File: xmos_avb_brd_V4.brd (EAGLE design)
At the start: 80 x 40 mm, 143 parts, among them IC1 IS25LP080D-JULE-TR_IS25LP080D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, J1 0826-1X1T-KL-F_0826-1X1T-KL-F, U1 AG9900_AG9905LP, U10 ST-MICROELECTRONICS2_ST1S06PUR, U2 AR8035_AR8035-AL1A-R, U3 XE216-512-TQ128-C20_XE216-512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, U4 ADM1085AKSZ-REEL7_ADM1085AKSZ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, U5 NC7WZ07P6X_NC7WZ07P6X, U6 CS2100-CP_CS2100-CP-CZZ, U7 ST-MICROELECTRONICS2_ST1S06PUR, U8 NCP303LSN30, U9 MIC5213-2.5V, X1 FA-238 25.000, X2 TC2050-XTAG_TC2050-NL-MCP-NL, X3 CON-MOLEX_52559-3092, X4 CON-MOLEX_52559-0692, Y1 ECS-3225Q-33-240-DP-TR_ECS-32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

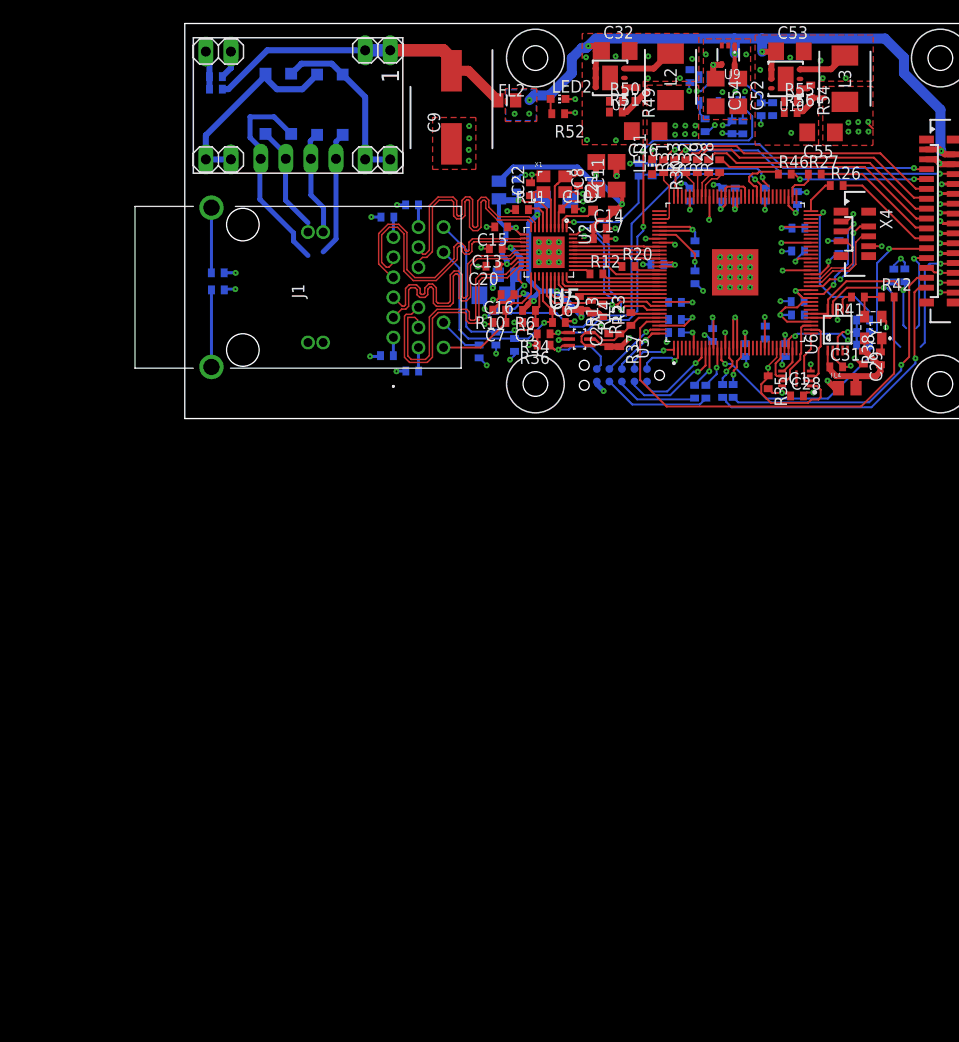
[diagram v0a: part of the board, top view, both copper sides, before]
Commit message: new debug header added to improve debugging with xmos. old tag-connect removed.
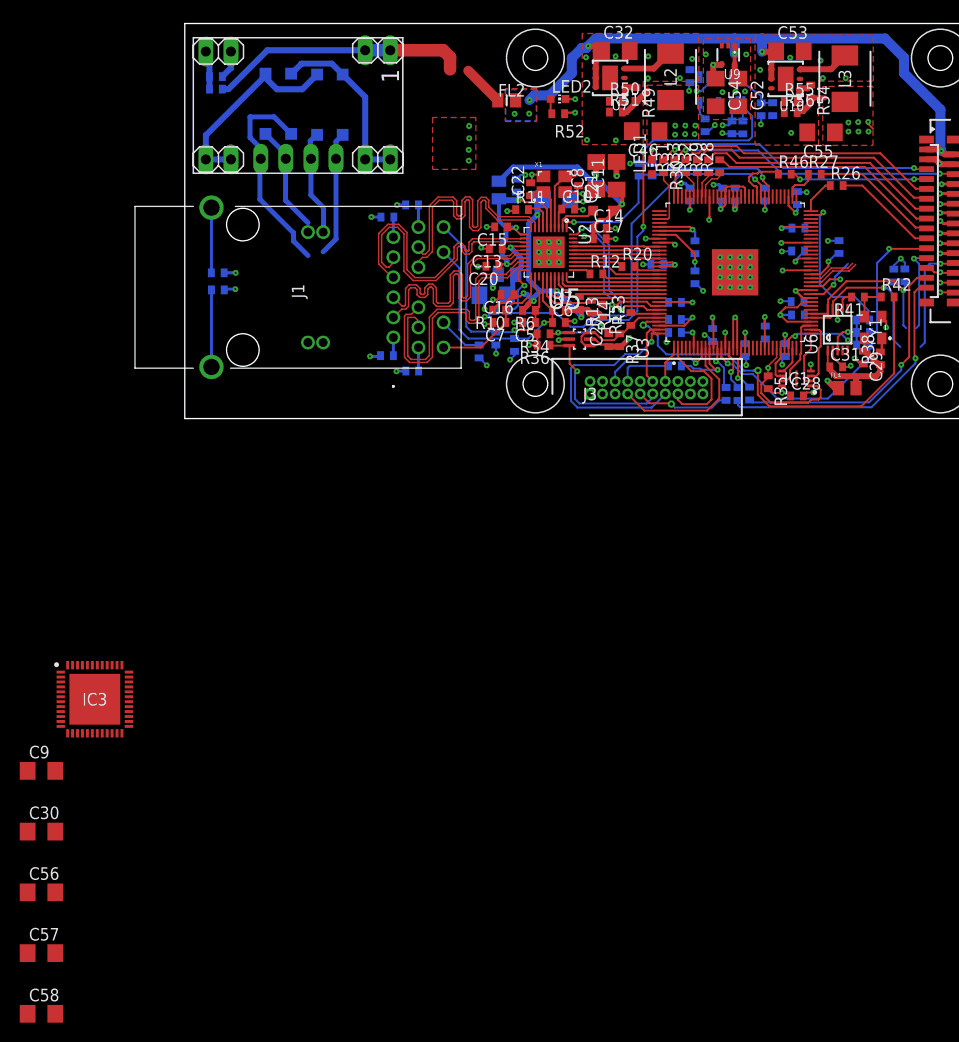
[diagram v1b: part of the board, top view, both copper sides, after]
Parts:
- removed X2: TC2050-XTAG_TC2050-NL-MCP-NL, xmos_avb_brd_V4:TC2050-XTAG_TC2030-MCP-NL
- removed X4: CON-MOLEX_52559-0692, xmos_avb_brd_V4:CON-MOLEX_52559-0692
- added C30, C56, C57, C58: 1u, xmos_avb_brd_V4:RCL_C1206
- added IC3: KSZ9131RNXI-TR, KSZ9131RNXI-TR:QFN50P700X700X90-49N
- added J3: ESHF-110-01-L-D-TH, ESHF-110-01-L-D-TH:SHDR20W41P127_2X10_1905X559X54
- C9: value EEH-ZC1V101P_EEH-ZC1V101P -> 1u; device xmos_avb_brd_V4:EEH-ZC1V101P_CAPAE830X1050N -> xmos_avb_brd_V4:RCL_C1206
- moved C9 79.0 mm to (-14.5, -35.7), turned to 0 degrees
- moved R24 3.29 mm to (49.6, 5.34), turned to 0 degrees
- moved R25 2.06 mm to (54.8, 2.50)
- moved R47 1.68 mm to (57.2, 2.52)
- moved R48 1.58 mm to (56.0, 2.48)
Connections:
- net GND: now also C30.2, C56.2, C57.2, C58.2, J3.10, J3.18, J3.3; no longer X2.5, X4.1, X4.6
- net TCK: now also J3.13; no longer X2.8
- net TDI: now also J3.15; no longer X2.10
- net TDO: now also J3.14; no longer X2.9
- net TMS: now also J3.12; no longer X2.7
- net USB_DM_N: now also J3.20; no longer X4.5
- net USB_DP_P: now also J3.19; no longer X4.4
- net USB_ID: now also J3.17; no longer X4.3
- net USB_VBUS: now also J3.16; no longer X4.2
- net VDC: now also C30.1, C56.1, C57.1, C58.1
- net XL_DN0: now also J3.7; no longer X2.2
- net XL_DN1: now also J3.6; no longer X2.1
- net XL_UP0: now also J3.8; no longer X2.3
- net XL_UP1: now also J3.9; no longer X2.4
- net XSYS_RST_N: now also J3.11; no longer X2.6
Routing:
- net TCK: track 5.63 -> 24.6 mm
- net XSYS_RST_N: track 8.57 -> 16.5 mm
- net USB_VBUS: track 10.3 -> 3.26 mm, vias 2 -> 1
- net TDI: track 5.18 -> 11.7 mm, vias 1 -> 0
- net USB_ID: track 11.3 -> 5.40 mm, vias 2 -> 1
- net GND: track 91.4 -> 86.1 mm, vias 112 -> 109
- net XL_DN0: track 11.0 -> 16.2 mm, vias 1 -> 0
- net USB_DP_P: track 9.08 -> 5.29 mm
- net XL_DN1: track 8.62 -> 11.7 mm
- net USB_DM_N: track 7.93 -> 4.88 mm
- net XL_UP0: track 8.31 -> 5.59 mm
- net N$43: track 4.49 -> 6.50 mm
- net VDC: track 32.4 -> 30.5 mm
- net SDIOE_OUT: track 29.5 -> 27.8 mm
- net TDO: track 5.50 -> 3.92 mm, vias 1 -> 0
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
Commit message: ksz9131 added to schematic.#
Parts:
- removed C16: 100n, xmos_avb_brd_V4:RCL_C0402
- removed C18, C19: 1u, xmos_avb_brd_V4:RCL_C1206
- removed L1: 4u7, xmos_avb_brd_V4:RCL_L2012C
- removed U2: AR8035_AR8035-AL1A-R, xmos_avb_brd_V4:AR8035_QFN40P500X500X75-41N
- added C59, C60, C64, C65, C69, C71, C72, C73: 100n, xmos_avb_brd_V4:RCL_C0402
- added C61, C62, C63, C66, C67, C68, C70: 10u, xmos_avb_brd_V4:RCL_C1206
- added FL5, FL6, FL7: BLM21AG471SN1D_BLM21AG471SN1D, xmos_avb_brd_V4:BLM21AG471SN1D_BEADC2012X105N
- added IC4: DMP2004K-7, DMP2004K-7:SOT96P240X110-3N
- added R57: 4R7, xmos_avb_brd_V4:RCL_R0402
- added R58: 6k04, xmos_avb_brd_V4:RCL_R0402
- added R59: 100k, xmos_avb_brd_V4:RCL_R0402
- added R60: 10k, xmos_avb_brd_V4:RCL_R0402
- added R61: 4k7, xmos_avb_brd_V4:RCL_R0402
- C11: value 10u -> 100n; device xmos_avb_brd_V4:RCL_C1206 -> xmos_avb_brd_V4:RCL_C0402
- C12: value 100n -> 10u; device xmos_avb_brd_V4:RCL_C0402 -> xmos_avb_brd_V4:RCL_C1206
- C5, C6, C7: value 470p -> 100n
- R10, R6, R7: value 10k -> 1k
- R11: value 2k37 -> 10k
- R15: value 1k5 -> 1k
- R5: value 510 -> 10k
- moved C7 220.3 mm to (-19.5, -204.5), turned to 0 degrees
- moved R11 217.7 mm to (-19.5, -189.8)
- moved R10 202.5 mm to (-19.5, -184.9), turned to 0 degrees
- moved R5 195.0 mm to (-19.5, -180.1), flipped to the top, turned to 0 degrees
- moved C6 193.6 mm to (-19.5, -175.2)
- moved C5 188.1 mm to (-19.5, -170.3), turned to 0 degrees
- moved C11 169.2 mm to (-15.5, -133.9), turned to 0 degrees
- moved C14 168.2 mm to (-15.5, -138.8)
- moved C58 106.5 mm to (31.7, 35.7), turned to 270 degrees
- moved C57 100.1 mm to (29.7, 35.7), turned to 270 degrees
- moved C56 92.8 mm to (25.6, 35.7), turned to 270 degrees
- moved C30 88.2 mm to (27.7, 35.7), turned to 270 degrees
- moved C13 85.7 mm to (-15.5, -54.5), turned to 0 degrees
- moved C9 80.8 mm to (23.4, 35.6), turned to 270 degrees
- moved C12 80.2 mm to (-14.5, -40.6), flipped to the top, turned to 0 degrees
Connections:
- removed net 1V1: C11.1, C14.1, C17.1, FL1.1, L1.2, U2.38
- removed net AVDD33: C13.1, C18.1, FL3.2, U2.14
- removed net VDDH_REG: C16.1, C19.1, R10.2, R13.2, R14.2, R15.2, R6.2, R7.2, U2.27, U2.8
- new net N$11: C59.1, FL5.1, IC3.44
- new net N$12: FL1.1
- new net N$17: C13.1, C60.1, C61.1, C62.1, C63.1, FL3.2, IC3.1, IC3.12, IC4.2, R59.1
- new net N$27: C17.1, C64.1, C65.1, C66.1, C67.1, C68.1, FL6.2, IC3.16, IC3.34, IC3.40
- new net N$31: IC3.48, R58.1
- new net N$32: IC4.1, R57.1, R59.2
- new net PHY_DVDDH: C7.1, R10.2, R11.2, R13.2, R14.2, R15.2, R5.2, R61.2
- new net PHY_VDD: C69.1, C70.1, C71.1, FL3.1, FL6.1
- new net PWR: C10.1, C11.1, C14.1, C72.1, C73.1, C8.1, FL7.1, IC3.18, IC3.23, IC3.26, IC3.30, IC3.39
- net 3V3: no longer C10.1, C8.1, FL3.1, R5.2, U2.3
- net AVDDL: now also FL5.2, FL7.2, IC3.4, IC3.9, IC4.3; no longer U2.11, U2.17, U2.6
- net GND: now also C59.2, IC3.29, IC3.49, R58.2, R6.1, R60.1, R7.1; no longer C11.2, C12.2, C13.2, C14.2, C16.2, C18.2, C19.2, C7.2, R11.1, U2.41
- net N$10: now also IC3.46; no longer U2.5
- net N$13: now also IC3.35; no longer U2.31
- net N$14: now also IC3.17, R7.2; no longer C7.1, R10.1, U2.21
- net N$20: now also IC3.41, R5.1; no longer R11.2, U2.7
- net N$3: now also IC3.43, R57.2; no longer L1.1, U2.2
- net N$54: now also IC3.15, R6.2; no longer C5.1, R5.1, R6.1, U2.22
- net N$6: no longer R7.1, U2.24
- net N$8: now also C5.1
- net N$9: now also IC3.45; no longer U2.4
- net PHY_INT: now also IC3.38, R61.1; no longer U2.20
- net PHY_MDC: now also IC3.36, R10.1; no longer U2.40
- net PHY_MDIO: now also IC3.37; no longer U2.39
- net PHY_RSTN: now also IC3.42; no longer U2.1
- net RX_D0: now also IC3.32, R60.2; no longer U2.29
- net RX_D1: now also IC3.31, R13.1; no longer U2.28
- net RX_D2: now also IC3.28, R14.1; no longer R13.1, U2.26
- net RX_D3: now also IC3.27, R11.1; no longer R14.1, U2.25
- net RX_DV: now also IC3.33; no longer U2.30
- net TRD1_N: now also IC3.3; no longer U2.10
- net TRD1_P: now also IC3.2; no longer U2.9
- net TRD2_N: now also IC3.6; no longer U2.13
- net TRD2_P: now also IC3.5; no longer U2.12
- net TRD3_N: now also IC3.8; no longer U2.16
- net TRD3_P: now also IC3.7; no longer U2.15
- net TRD4_N: now also IC3.11; no longer U2.19
- net TRD4_P: now also IC3.10; no longer U2.18
- net TX_CLK: now also IC3.24; no longer U2.33
- net TX_D0: now also IC3.19; no longer U2.34
- net TX_D1: now also IC3.20; no longer U2.35
- net TX_D2: now also IC3.21; no longer U2.36
- net TX_D3: now also IC3.22; no longer U2.37
- net TX_EN: now also IC3.25; no longer U2.32
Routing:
- net VDDH_REG: track 31.9 -> 0.00 mm, vias 5 -> 1
- net PHY_RSTN: track 27.0 -> 0.00 mm, vias 2 -> 0
- net 1V1: track 24.2 -> 0.00 mm, vias 1 -> 0
- net GND: track 86.1 -> 71.4 mm, vias 109 -> 88
- net AVDDL: track 21.7 -> 7.88 mm, vias 3 -> 2
- net N$14: track 13.6 -> 0.00 mm
- net 3V3: track 72.8 -> 63.2 mm, vias 32 -> 29
- net N$54: track 23.7 -> 14.2 mm, vias 1 -> 0
- net TX_D3: track 8.76 -> 0.00 mm
- net AVDD33: track 8.42 -> 0.00 mm, vias 1 -> 0
- net RX_D3: track 13.9 -> 6.65 mm
- net TX_D2: track 8.76 -> 1.61 mm
- net TX_D0: track 8.76 -> 1.63 mm
- net TX_D1: track 8.76 -> 1.64 mm
- net VDC: track 30.5 -> 24.0 mm
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
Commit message: layout wip
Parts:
- removed C52, C54, C57: 1u, xmos_avb_brd_V4:RCL_C1206
- removed C70: 10u, xmos_avb_brd_V4:RCL_C1206
- removed FL1: BLM21AG471SN1D_BLM21AG471SN1D, xmos_avb_brd_V4:BLM21AG471SN1D_BEADC2012X105N
- removed U9: MIC5213-2.5V, xmos_avb_brd_V4:MICREL2_SC70-5
- added C16, C18, C19: 10u, xmos_avb_brd_V4:RCL_C1206
- C30: value 1u -> 100n; device xmos_avb_brd_V4:RCL_C1206 -> xmos_avb_brd_V4:RCL_C0402
- C32, C53: value 4u7 -> 10u
- C46, C55: value 22u -> 10u
- C56, C58, C9: value 1u -> 10u
- FL3, FL5, FL6, FL7: value BLM21AG471SN1D_BLM21AG471SN1D -> 742792711; device xmos_avb_brd_V4:BLM21AG471SN1D_BEADC2012X105N -> 742792711:0402
- moved C7 243.0 mm to (40.5, 31.0), flipped to the bottom, turned to 90 degrees
- moved R61 233.2 mm to (39.7, 25.9), turned to 90 degrees
- moved R60 226.3 mm to (45.0, 22.1), flipped to the bottom
- moved R10 219.6 mm to (41.9, 25.9), turned to 90 degrees
- moved R11 218.4 mm to (45.0, 18.8), flipped to the bottom, turned to 180 degrees
- moved R5 213.5 mm to (36.5, 25.9), turned to 90 degrees
- moved IC4 196.6 mm to (27.5, 25.8), turned to 180 degrees
- moved C6 193.5 mm to (29.6, 12.0), turned to 270 degrees
- moved R59 189.7 mm to (29.9, 25.9), turned to 270 degrees
- moved C5 185.9 mm to (29.6, 9.02), turned to 270 degrees
- moved R58 185.7 mm to (32.4, 25.9), turned to 90 degrees
- moved C72 173.4 mm to (41.3, 20.1), flipped to the bottom, turned to 180 degrees
- moved C73 170.3 mm to (37.4, 13.3), flipped to the bottom, turned to 270 degrees
- moved C71 166.6 mm to (41.7, 31.0), flipped to the bottom, turned to 90 degrees
- moved C14 163.9 mm to (40.4, 15.3), flipped to the bottom, turned to 270 degrees
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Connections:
- net N$11 renamed AVDDL_PLL
- net N$17 renamed AVDDH
- net N$3 renamed LDO
- net PWR renamed DVDDL
- removed net 2V5: C33.1, C54.1, U3.110, U3.111, U9.4
- removed net N$12: FL1.1
- removed net N$27: C17.1, C64.1, C65.1, C66.1, C67.1, C68.1, FL6.2, IC3.16, IC3.34, IC3.40
- removed net PHY_DVDDH: C7.1, R10.2, R11.2, R13.2, R14.2, R15.2, R5.2, R61.2
- removed net PHY_VDD: C69.1, C70.1, C71.1, FL3.1, FL6.1
- new net DVDDH: C17.1, C64.1, C65.1, C66.1, C67.1, C68.1, C7.1, FL6.2, IC3.16, IC3.34, IC3.40, R10.2, R11.2, R13.2, R14.2, R15.2, R5.2, R61.2
- new net PHY_VDD_3V3: C33.1, C69.1, C71.1, FL3.1, FL6.1, U3.110, U3.111
- net 1V0: now also C19.1
- net 3V3: now also C16.1, C18.1
- net 5V0: no longer C52.1, U9.1, U9.5
- net AVDDL: no longer FL1.2
- net GND: now also C11.2, C12.2, C13.2, C14.2, C16.2, C18.2, C19.2, C60.2, C61.2, C62.2, C63.2, C64.2, C65.2, C66.2, C67.2, C68.2, C69.2, C7.2, C71.2, C72.2, C73.2; no longer C30.2, C52.2, C54.2, C57.2, U9.3
- net VDC: no longer C30.1, C57.1
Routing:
- net DVDDH: track 0.00 -> 50.0 mm, vias 0 -> 7
- net DVDDL: track 4.59 -> 43.6 mm, vias 1 -> 6
- net PHY_VDD_3V3: track 0.00 -> 35.8 mm, vias 0 -> 2
- net 2V5: track 29.5 -> 0.00 mm, vias 2 -> 0
- net PHY_INT: track 42.1 -> 13.2 mm
- net AVDDH: track 0.00 -> 27.1 mm, vias 0 -> 4
- net GND: track 71.4 -> 98.4 mm, vias 88 -> 135
- net N$14: track 0.00 -> 19.1 mm
- net AVDDL: track 7.88 -> 23.5 mm, vias 2 -> 6
- net TX_D0: track 1.63 -> 16.7 mm, vias 0 -> 2
- net PHY_RSTN: track 0.00 -> 14.9 mm, vias 0 -> 2
- net TX_D3: track 0.00 -> 14.4 mm, vias 0 -> 2
- net TX_D1: track 1.64 -> 15.9 mm, vias 0 -> 2
- net TX_D2: track 1.61 -> 15.1 mm, vias 0 -> 2
- net TRD1_P: track 26.8 -> 13.6 mm
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- removed copper zone on layer 1, net 5V0
- removed copper zone on layer 16, net 5V0
